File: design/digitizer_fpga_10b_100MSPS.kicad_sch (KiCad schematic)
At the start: 4 parts

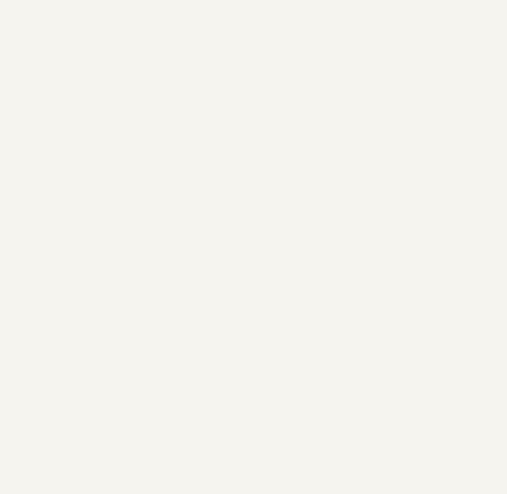
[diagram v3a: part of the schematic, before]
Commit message: Added logo and description to F.Silks
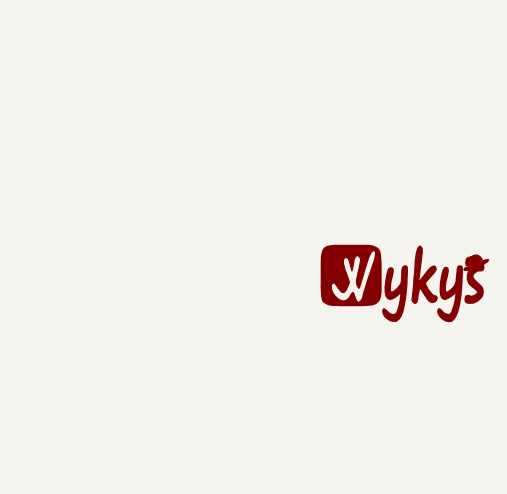
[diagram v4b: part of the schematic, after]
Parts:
- added GR1: Wykys, KLIB_Logo:wykys_small_skill, symbol KLIB_Logo:Wykys
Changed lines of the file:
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@@
-(kicad_sch (version 20200512) (host eeschema "5.99.0-unknown-d72a778~101~ubuntu18.04.1")
+(kicad_sch (version 20200512) (host eeschema "5.99.0-unknown-4efed4b~101~ubuntu18.04.1")
   (page 1 8)
   (paper "A4")
@@
     )
   )
+  (symbol (lib_id "KLIB_Logo:Wykys") (at 271.78 173.99 0) (unit 1)
+    (property "Reference" "GR1" (id 0) (at 271.78 177.4444 0)
+      (effects (font (size 1.27 1.27)) hide)
+    )
+    (property "Value" "Wykys" (id 1) (at 271.78 170.5356 0)
+      (effects (font (size 1.27 1.27)) hide)
+    )
+    (property "Footprint" "KLIB_Logo:wykys_small_skill" (id 2) (at 271.78 180.34 0)
+      (effects (font (size 1.27 1.27)) hide)
+    )
+    (property "Datasheet" "https://github.com/wykys" (id 3) (at 271.78 177.4444 0)
+      (effects (font (size 1.27 1.27)) hide)
+    )
+  )
   (sheet (at 154.94 99.06) (size 22.86 12.7)
     (stroke (width 0.1524) (color 198 120 221 1))
@@
     (path "/6c07a7e5-f136-44bb-8086-ba05ad45ce64" (reference "#PWR03") (unit 1))
     (path "/f54593db-a2df-44c5-8513-2bde6eaa3b94" (reference "#PWR04") (unit 1))
+    (path "/0986990b-68f7-46ae-983b-508b0be78074" (reference "GR1") (unit 1))
     (path "/f56eaa1e-ba52-456d-99dd-e4fffeedc129" (reference "H1") (unit 1))
     (path "/046fc9d9-8dfd-4c80-b086-7203e50e39fb" (reference "H2") (unit 1))

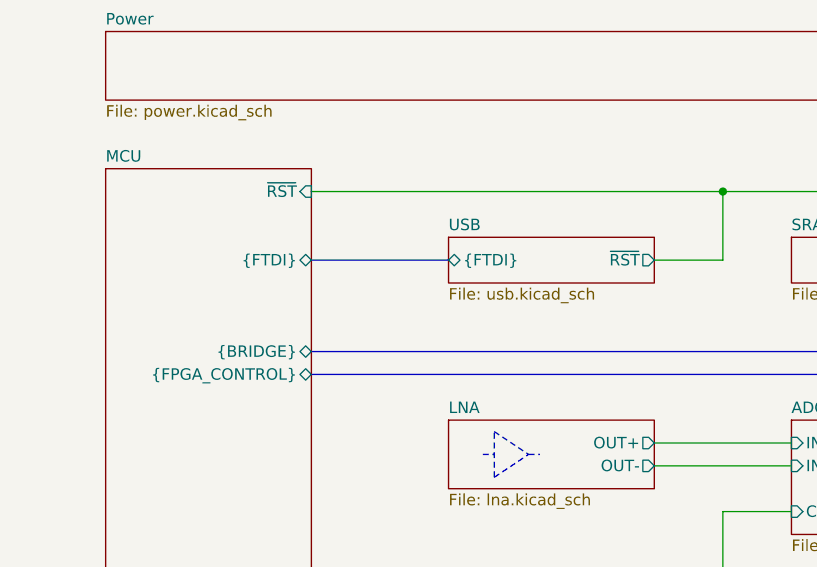
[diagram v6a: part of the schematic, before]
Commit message: Updated reset system
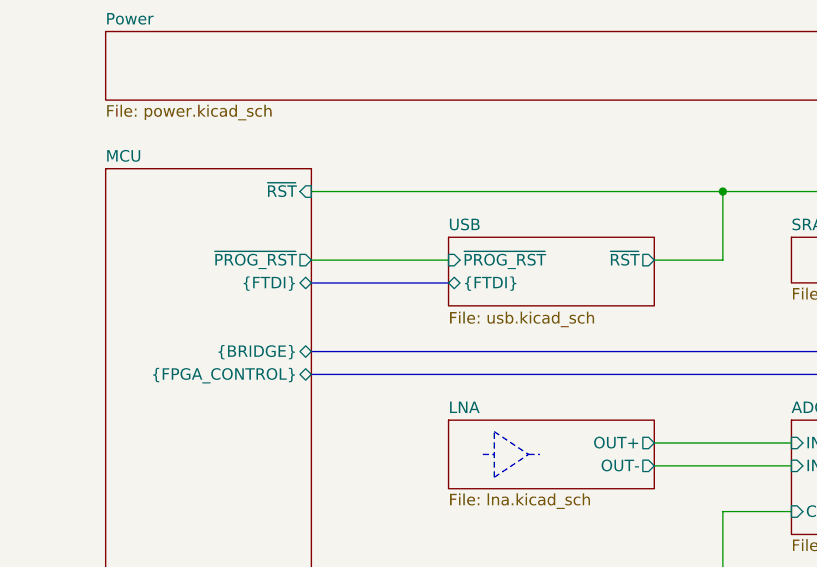
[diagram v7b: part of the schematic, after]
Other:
- sheet MCU ports: added ~PROG_RST; removed none
- sheet USB ports: added ~PROG_RST; removed none
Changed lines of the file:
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@@
   (junction (at 147.32 116.84))
   (wire (pts (xy 101.6 73.66) (xy 147.32 73.66)))
+  (wire (pts (xy 101.6 81.28) (xy 116.84 81.28)))
   (wire (pts (xy 101.6 116.84) (xy 147.32 116.84)))
   (wire (pts (xy 139.7 81.28) (xy 147.32 81.28)))
@@
   (wire (pts (xy 147.32 116.84) (xy 193.04 116.84)))
   (wire (pts (xy 154.94 109.22) (xy 147.32 109.22)))
-  (bus (pts (xy 101.6 81.28) (xy 116.84 81.28)))
+  (bus (pts (xy 101.6 83.82) (xy 116.84 83.82)))
   (bus (pts (xy 101.6 91.44) (xy 193.04 91.44)))
   (bus (pts (xy 101.6 93.98) (xy 193.04 93.98)))
@@
       (effects (font (size 1.27 1.27)) (justify right))
     )
-    (pin "{FTDI}" bidirectional (at 101.6 81.28 0)
+    (pin "{FTDI}" bidirectional (at 101.6 83.82 0)
       (effects (font (size 1.27 1.27)) (justify right))
     )
@@
       (effects (font (size 1.27 1.27)) (justify right))
     )
+    (pin "~PROG_RST" output (at 101.6 81.28 0)
+      (effects (font (size 1.27 1.27)) (justify right))
+    )
   )
   (sheet (at 78.74 55.88) (size 137.16 7.62)
@@
     )
   )
-  (sheet (at 116.84 78.74) (size 22.86 5.08)
+  (sheet (at 116.84 78.74) (size 22.86 7.62)
     (stroke (width 0.1524) (color 198 120 221 1))
     (fill (color 0 0 0 1.0000))
@@
       (effects (font (size 1.27 1.27)) (justify left bottom))
     )
-    (property "Sheet file" "usb.kicad_sch" (id 1) (at 116.84 84.3285 0)
-      (effects (font (size 1.27 1.27)) (justify left top))
-    )
-    (pin "{FTDI}" bidirectional (at 116.84 81.28 180)
+    (property "Sheet file" "usb.kicad_sch" (id 1) (at 116.84 86.995 0)
+      (effects (font (size 1.27 1.27)) (justify left top))
+    )
+    (pin "{FTDI}" bidirectional (at 116.84 83.82 180)
       (effects (font (size 1.27 1.27)) (justify left))
     )
     (pin "~RST" output (at 139.7 81.28 0)
       (effects (font (size 1.27 1.27)) (justify right))
+    )
+    (pin "~PROG_RST" input (at 116.84 81.28 180)
+      (effects (font (size 1.27 1.27)) (justify left))
     )
   )
@@
     (path "/744549a0-bc16-487f-9ead-074cadabfe5e/19da8a86-1fe2-482a-992a-e211b8b8d41e" (reference "J3") (unit 1))
     (path "/744549a0-bc16-487f-9ead-074cadabfe5e/78594602-2556-4f27-ac12-3b4da0d3bb65" (reference "R14") (unit 1))
-    (path "/744549a0-bc16-487f-9ead-074cadabfe5e/d90b3eeb-69cf-41d6-96c1-116326f4bef1" (reference "R15") (unit 1))
     (path "/744549a0-bc16-487f-9ead-074cadabfe5e/244447f5-df02-4d27-bb03-893eb2479e14" (reference "R16") (unit 1))
     (path "/744549a0-bc16-487f-9ead-074cadabfe5e/b557b616-2960-4c03-a9a3-c92ff4e53aa9" (reference "R17") (unit 1))
@@
     (path "/9c26d541-ff6a-4a88-8a78-9a95fd5b0d69/d7e2bb3e-79ee-43b9-8cbd-52d52ecb448f" (reference "#PWR096") (unit 1))
     (path "/9c26d541-ff6a-4a88-8a78-9a95fd5b0d69/0a7fdb68-87dd-4354-bdac-bfa620629cee" (reference "#PWR097") (unit 1))
-    (path "/9c26d541-ff6a-4a88-8a78-9a95fd5b0d69/aeb5d38c-c070-43ee-9276-b279db2e7ae0" (reference "#PWR098") (unit 1))
-    (path "/9c26d541-ff6a-4a88-8a78-9a95fd5b0d69/28f61018-2d76-437b-bc50-c0da039a0b3a" (reference "#PWR099") (unit 1))
+    (path "/9c26d541-ff6a-4a88-8a78-9a95fd5b0d69/03ec8dff-3f1f-452e-a043-c8b49b92eb71" (reference "#PWR098") (unit 1))
+    (path "/9c26d541-ff6a-4a88-8a78-9a95fd5b0d69/c3154044-e33e-435f-bdd5-cd3f7fa9e27b" (reference "#PWR099") (unit 1))
     (path "/9c26d541-ff6a-4a88-8a78-9a95fd5b0d69/a7c6af8e-6a43-4e2a-8f08-5dc641f9b221" (reference "#PWR0100") (unit 1))
-    (path "/9c26d541-ff6a-4a88-8a78-9a95fd5b0d69/5e4dd8e5-922f-4a58-8832-85ae6c3a21da" (reference "#PWR0101") (unit 1))
-    (path "/9c26d541-ff6a-4a88-8a78-9a95fd5b0d69/b88c5173-1f25-4570-ae24-5836c3b4da13" (reference "#PWR0102") (unit 1))
+    (path "/9c26d541-ff6a-4a88-8a78-9a95fd5b0d69/d01101a9-3142-49a7-ae1b-4c474d8fe288" (reference "#PWR0101") (unit 1))
+    (path "/9c26d541-ff6a-4a88-8a78-9a95fd5b0d69/790bd3ea-947f-40bb-8688-04ea295480ee" (reference "#PWR0102") (unit 1))
     (path "/9c26d541-ff6a-4a88-8a78-9a95fd5b0d69/8d7f344b-5e73-44c4-8882-3fe90aef13d5" (reference "#PWR0103") (unit 1))
     (path "/9c26d541-ff6a-4a88-8a78-9a95fd5b0d69/a3c5eba2-74fe-4f34-86e2-b5b675a854ba" (reference "#PWR0104") (unit 1))
@@
     (path "/9c26d541-ff6a-4a88-8a78-9a95fd5b0d69/9183b50d-231c-403f-abcd-25c130aa0ca0" (reference "#PWR0106") (unit 1))
     (path "/9c26d541-ff6a-4a88-8a78-9a95fd5b0d69/83f61411-f6ee-4360-b7e0-804387c15179" (reference "#PWR0107") (unit 1))
+    (path "/9c26d541-ff6a-4a88-8a78-9a95fd5b0d69/8473118c-ac12-4c40-b72c-c7d0091856d7" (reference "#PWR0220") (unit 1))
+    (path "/9c26d541-ff6a-4a88-8a78-9a95fd5b0d69/e6352665-69e7-4550-861d-7a1d0b4c9d21" (reference "#PWR0221") (unit 1))
     (path "/9c26d541-ff6a-4a88-8a78-9a95fd5b0d69/6d8f14d9-b258-4b90-b74d-88080ddd6996" (reference "C45") (unit 1))
     (path "/9c26d541-ff6a-4a88-8a78-9a95fd5b0d69/b88e69c5-ed03-4b6f-98ac-0068c5bd15f9" (reference "C46") (unit 1))
     (path "/9c26d541-ff6a-4a88-8a78-9a95fd5b0d69/7c677dca-15ff-438d-a224-a4cf7ac61ab6" (reference "C47") (unit 1))
     (path "/9c26d541-ff6a-4a88-8a78-9a95fd5b0d69/7afedc8b-b3d4-496f-aaed-36e0fcda2d85" (reference "C48") (unit 1))
-    (path "/9c26d541-ff6a-4a88-8a78-9a95fd5b0d69/37c5d65f-741d-47cf-9097-b632843f63d6" (reference "C49") (unit 1))
+    (path "/9c26d541-ff6a-4a88-8a78-9a95fd5b0d69/25123af5-736d-4101-b13c-5cc7319f98e5" (reference "C49") (unit 1))
     (path "/9c26d541-ff6a-4a88-8a78-9a95fd5b0d69/66cd0ec2-ad09-491e-9eb0-dfb278a81c01" (reference "C50") (unit 1))
     (path "/9c26d541-ff6a-4a88-8a78-9a95fd5b0d69/2bb32e5a-3a8a-43c1-9c92-6456c7d23081" (reference "C51") (unit 1))
     (path "/9c26d541-ff6a-4a88-8a78-9a95fd5b0d69/26441dbd-ce15-4f85-b25b-f1ecfb153a90" (reference "C52") (unit 1))
     (path "/9c26d541-ff6a-4a88-8a78-9a95fd5b0d69/17de9513-e210-4fbf-bf1c-9e99ca629f23" (reference "J4") (unit 1))
+    (path "/9c26d541-ff6a-4a88-8a78-9a95fd5b0d69/4f21c704-edba-4f03-96de-36d3f8e2369f" (reference "JP1") (unit 1))
     (path "/9c26d541-ff6a-4a88-8a78-9a95fd5b0d69/23c6f1cf-6340-457e-91db-1e78a6b55334" (reference "R25") (unit 1))
     (path "/9c26d541-ff6a-4a88-8a78-9a95fd5b0d69/02507687-d084-4c8f-81a3-8bb30ff2a2f7" (reference "R26") (unit 1))
@@
     (path "/9c26d541-ff6a-4a88-8a78-9a95fd5b0d69/f94c70c4-3a57-4570-b969-49041b8a9ec1" (reference "R34") (unit 1))
     (path "/9c26d541-ff6a-4a88-8a78-9a95fd5b0d69/339e2547-2ca4-4cac-91eb-3a1218e3ce03" (reference "R35") (unit 1))
+    (path "/9c26d541-ff6a-4a88-8a78-9a95fd5b0d69/12658567-64a6-4926-a10a-4bebd28cc930" (reference "R130") (unit 1))
+    (path "/9c26d541-ff6a-4a88-8a78-9a95fd5b0d69/9c84b958-0114-475f-9d8c-9f79297819aa" (reference "R131") (unit 1))
     (path "/9c26d541-ff6a-4a88-8a78-9a95fd5b0d69/db54fdd4-fe51-476e-b56e-564980a48a88" (reference "SW1") (unit 1))
-    (path "/9c26d541-ff6a-4a88-8a78-9a95fd5b0d69/641cf1da-71d9-4c4f-9ba7-2ac0f7b50ad5" (reference "U7") (unit 1))
+    (path "/9c26d541-ff6a-4a88-8a78-9a95fd5b0d69/d2f93ab6-c29f-43f0-9e5d-01669b2c5260" (reference "U7") (unit 1))
     (path "/9c26d541-ff6a-4a88-8a78-9a95fd5b0d69/8c76e81f-c189-4f87-a53c-e84baad1a467" (reference "U8") (unit 1))
     (path "/9c26d541-ff6a-4a88-8a78-9a95fd5b0d69/76e4f4dd-e131-47c5-a73e-0051c21fe421" (reference "U9") (unit 1))

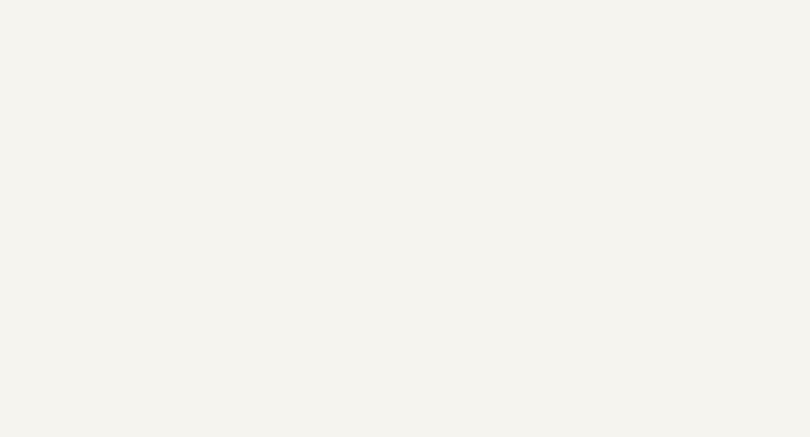
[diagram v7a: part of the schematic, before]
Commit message: Added fiducials
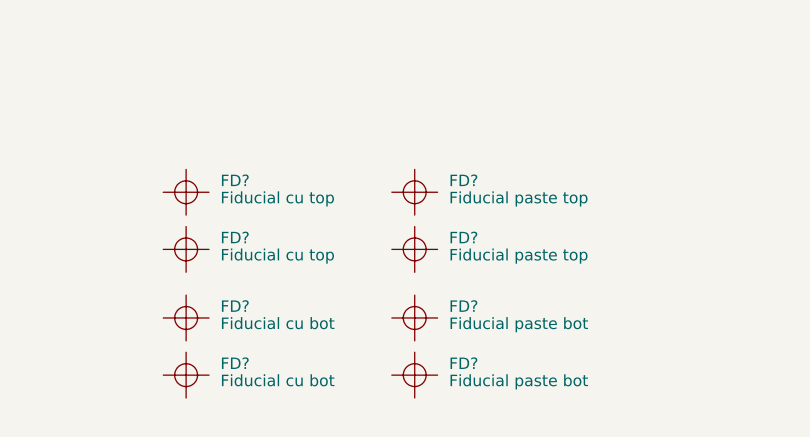
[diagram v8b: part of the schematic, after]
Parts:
- added FD? (x2): Fiducial paste top, KLIB_Mechanical:Fiducial_Paste_Pad_1.5mm_Outer_2.5mm, symbol KLIB_Mechanical:Fiducial
- added FD? (x2): Fiducial cu bot, KLIB_Mechanical:Fiducial_Pad_1.5mm_Outer_2.5mm, symbol KLIB_Mechanical:Fiducial
- added FD? (x2): Fiducial paste bot, KLIB_Mechanical:Fiducial_Paste_Pad_1.5mm_Outer_2.5mm, symbol KLIB_Mechanical:Fiducial
- added FD? (x2): Fiducial cu top, KLIB_Mechanical:Fiducial_Pad_1.5mm_Outer_2.5mm, symbol KLIB_Mechanical:Fiducial
